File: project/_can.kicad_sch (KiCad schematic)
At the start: 11 parts, among them U501 XL1050

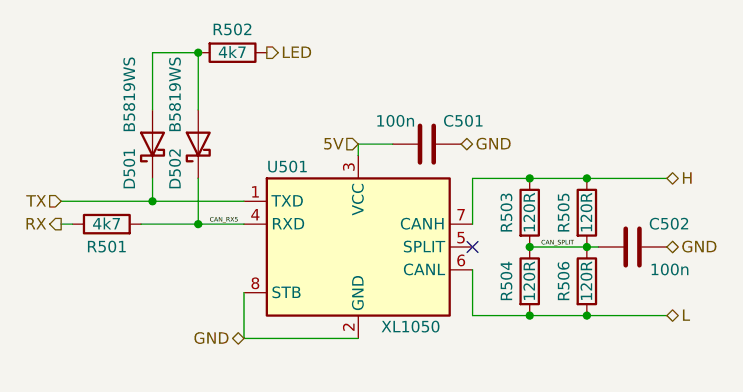
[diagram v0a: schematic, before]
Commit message: CAN resistors, power wires and version bump
* fixing CAN level shifting resistors
* exposing more copper for power wires between boards
* bumping up version
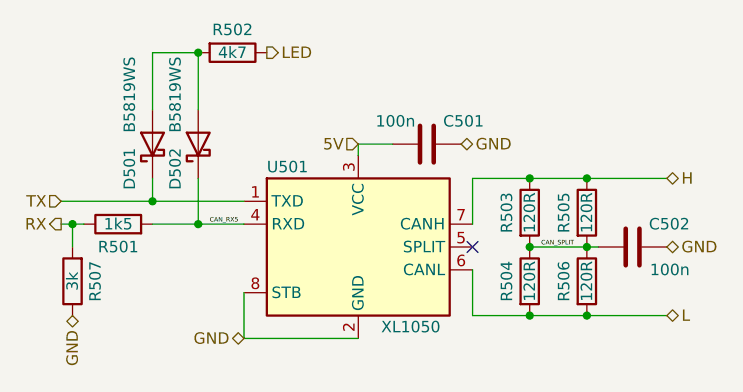
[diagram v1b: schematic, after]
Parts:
- added R507: 3k, Resistor_SMD:R_0402_1005Metric_Pad0.72x0.64mm_HandSolder, symbol Device:R
- R501: value 4k7 -> 1k5; lcsc# C25900 -> C4310
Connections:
- net GND: now also R507.1
- net RX: now also R507.2
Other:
- moved on the sheet: R501
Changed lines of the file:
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@@
   (junction (at 143.51 104.14) (diameter 0) (color 0 0 0 0)
+  )
+  (junction (at 92.71 93.98) (diameter 0) (color 0 0 0 0)
   )
   (no_connect (at 137.16 96.52))
@@
     (stroke (width 0) (type default) (color 0 0 0 0))
   )
-  (wire (pts (xy 100.33 93.98) (xy 106.68 93.98))
+  (wire (pts (xy 101.6 93.98) (xy 106.68 93.98))
     (stroke (width 0) (type default) (color 0 0 0 0))
   )
@@
     (stroke (width 0) (type default) (color 0 0 0 0))
   )
+  (wire (pts (xy 92.71 93.98) (xy 93.98 93.98))
+    (stroke (width 0) (type default) (color 0 0 0 0))
+  )
   (wire (pts (xy 91.44 91.44) (xy 101.6 91.44))
     (stroke (width 0) (type default) (color 0 0 0 0))
@@
   )
   (wire (pts (xy 124.46 85.09) (xy 124.46 86.36))
+    (stroke (width 0) (type default) (color 0 0 0 0))
+  )
+  (wire (pts (xy 92.71 93.98) (xy 92.71 96.52))
     (stroke (width 0) (type default) (color 0 0 0 0))
   )
@@
   )
   (hierarchical_label "GND" (shape bidirectional) (at 111.76 106.68 180)
+    (effects (font (size 1.27 1.27)) (justify right))
+  )
+  (hierarchical_label "GND" (shape bidirectional) (at 92.71 104.14 270)
     (effects (font (size 1.27 1.27)) (justify right))
   )
@@
     (pin "2")
   )
-  (symbol (lib_id "Device:R") (at 96.52 93.98 90) (unit 1)
-    (in_bom yes) (on_board yes)
-    (property "Reference" "R501" (id 0) (at 96.52 96.52 90))
-    (property "Value" "4k7" (id 1) (at 96.52 93.98 90))
-    (property "Footprint" "Resistor_SMD:R_0402_1005Metric_Pad0.72x0.64mm_HandSolder" (id 2) (at 96.52 95.758 90)
-      (effects (font (size 1.27 1.27)) hide)
-    )
-    (property "Datasheet" "~" (id 3) (at 96.52 93.98 0)
-      (effects (font (size 1.27 1.27)) hide)
-    )
-    (property "jlc-part-type" "B+" (id 4) (at 96.52 93.98 0)
-      (effects (font (size 1.27 1.27)) hide)
-    )
-    (property "lcsc#" "C25900" (id 5) (at 96.52 93.98 0)
+  (symbol (lib_id "Device:R") (at 97.79 93.98 90) (unit 1)
+    (in_bom yes) (on_board yes)
+    (property "Reference" "R501" (id 0) (at 97.79 96.52 90))
+    (property "Value" "1k5" (id 1) (at 97.79 93.98 90))
+    (property "Footprint" "Resistor_SMD:R_0402_1005Metric_Pad0.72x0.64mm_HandSolder" (id 2) (at 97.79 95.758 90)
+      (effects (font (size 1.27 1.27)) hide)
+    )
+    (property "Datasheet" "~" (id 3) (at 97.79 93.98 0)
+      (effects (font (size 1.27 1.27)) hide)
+    )
+    (property "jlc-part-type" "B+" (id 4) (at 97.79 93.98 0)
+      (effects (font (size 1.27 1.27)) hide)
+    )
+    (property "lcsc#" "C4310" (id 5) (at 97.79 93.98 0)
       (effects (font (size 1.27 1.27)) hide)
     )
@@
       (effects (font (size 1.27 1.27)) hide)
     )
+    (pin "1")
+    (pin "2")
+  )
+  (symbol (lib_id "Device:R") (at 92.71 100.33 180) (unit 1)
+    (in_bom yes) (on_board yes)
+    (property "Reference" "R507" (id 0) (at 95.25 100.33 90))
+    (property "Value" "3k" (id 1) (at 92.71 100.33 90))
+    (property "Footprint" "Resistor_SMD:R_0402_1005Metric_Pad0.72x0.64mm_HandSolder" (id 2) (at 94.488 100.33 90)
+      (effects (font (size 1.27 1.27)) hide)
+    )
+    (property "Datasheet" "~" (id 3) (at 92.71 100.33 0)
+      (effects (font (size 1.27 1.27)) hide)
+    )
+    (property "jlc-part-type" "B+" (id 4) (at 92.71 100.33 0)
+      (effects (font (size 1.27 1.27)) hide)
+    )
+    (property "lcsc#" "C17661" (id 5) (at 92.71 100.33 0)
+      (effects (font (size 1.27 1.27)) hide)
+    )
